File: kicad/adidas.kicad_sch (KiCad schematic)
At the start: 21 parts, among them J1 ISP Header, J2 Conn_01x02_Female, J3 SAO Header, U1 MPU-6050, U2 ATTINY841-SSU

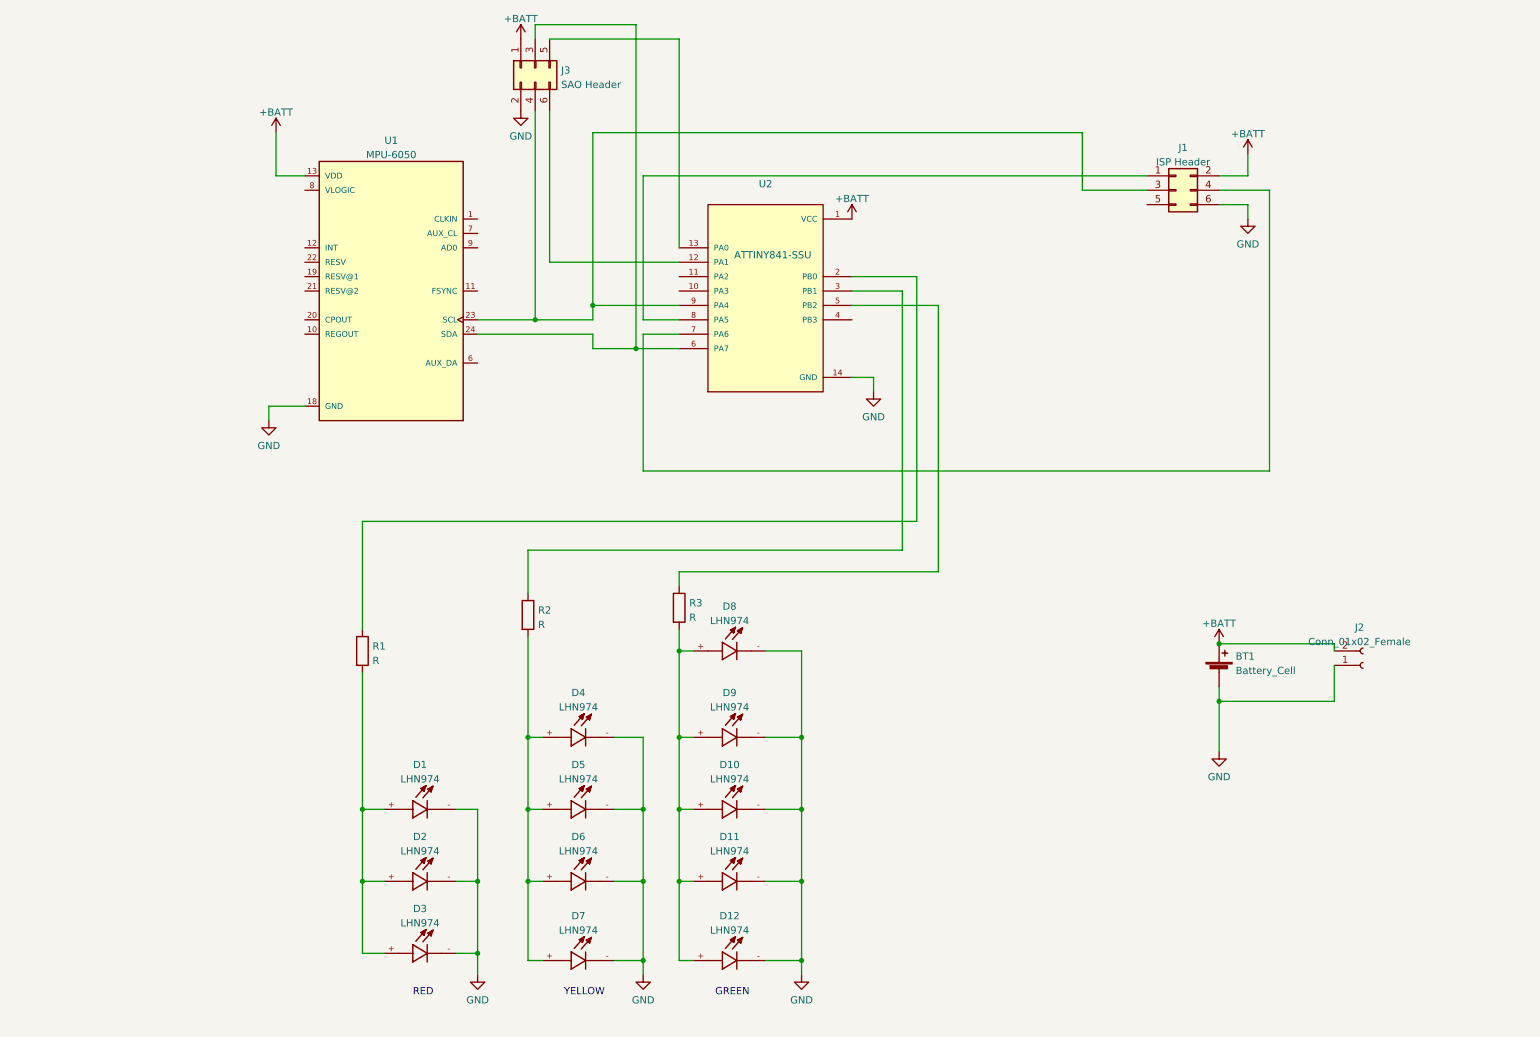
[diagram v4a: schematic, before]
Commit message: changes after feedback from PCBway
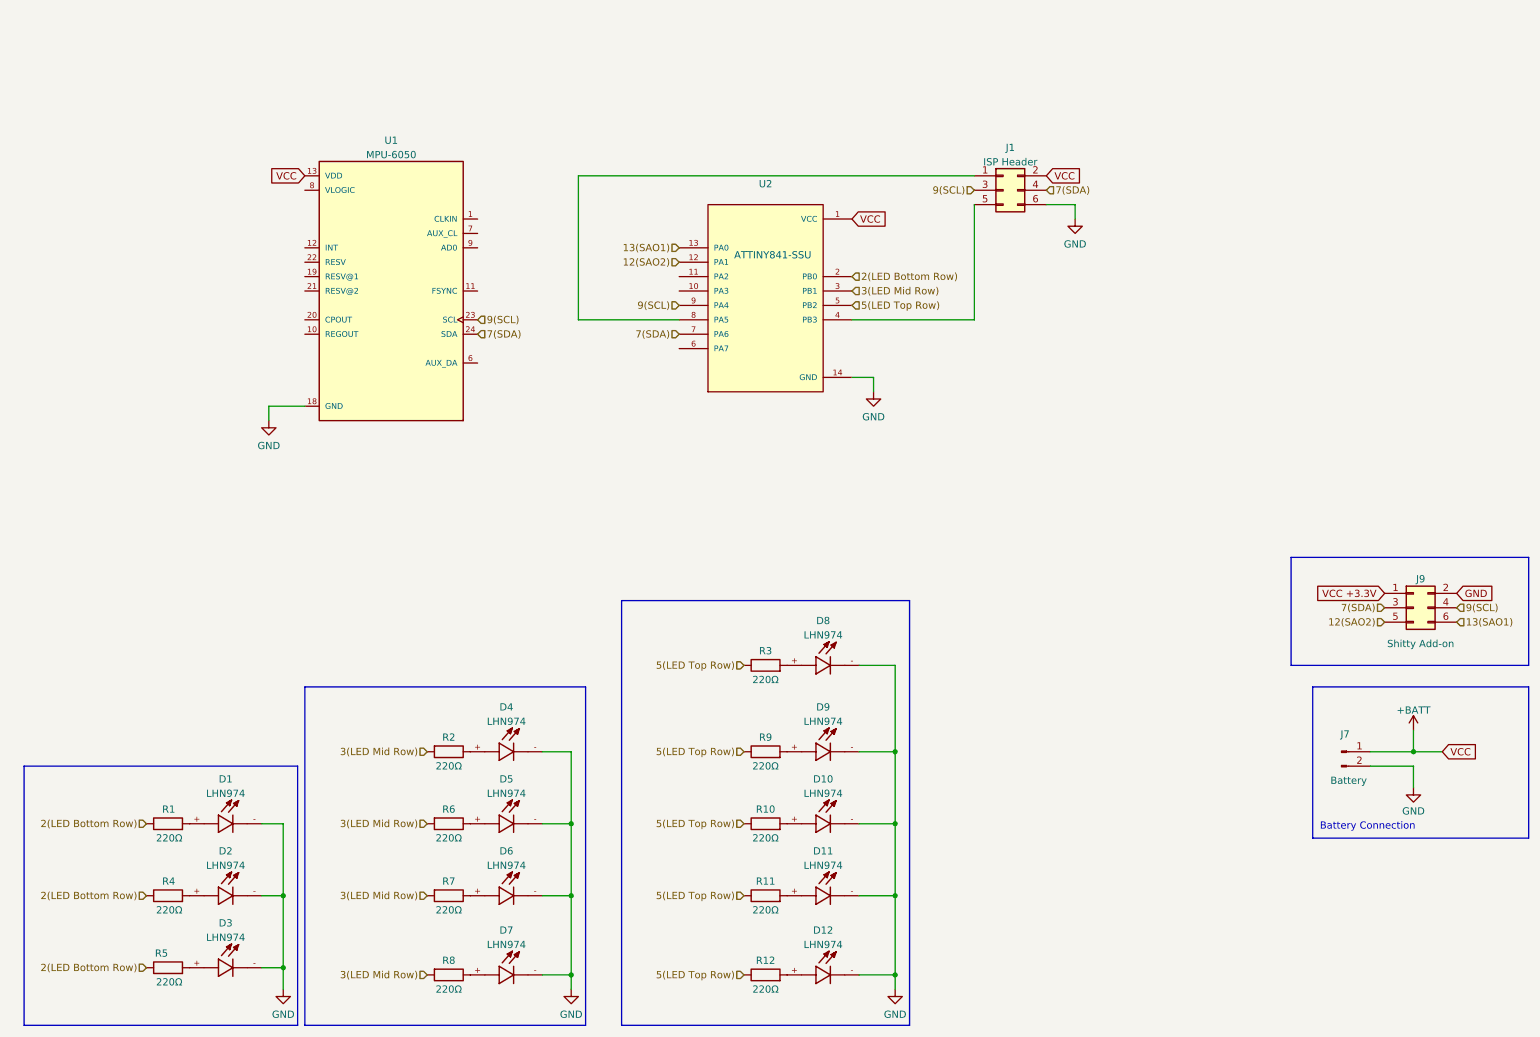
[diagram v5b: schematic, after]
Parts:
- removed BT1: Battery_Cell, Battery:BatteryHolder_Keystone_3002_1x2032, symbol Device:Battery_Cell
- removed J2: Conn_01x02_Female, TestPoint:TestPoint_2Pads_Pitch2.54mm_Drill0.8mm, symbol Connector:Conn_01x02_Female
- removed J3: SAO Header, Connector_PinHeader_2.54mm:PinHeader_2x03_P2.54mm_Vertical, symbol Connector_Generic:Conn_02x03_Odd_Even
- added J7: Battery, Connector_PinSocket_2.54mm:PinSocket_1x02_P2.54mm_Vertical, symbol Connector:Conn_01x02_Pin
- added J9: Shitty Add-on, Connector_PinHeader_2.54mm:PinHeader_2x03_P2.54mm_Vertical, symbol Connector_Generic:Conn_02x03_Odd_Even
- added R10, R11, R12, R4, R5, R6, R7, R8, R9: 220Ω, Resistor_SMD:R_1206_3216Metric, symbol Device:R
- D1, D10, D11, D12, D2, D3, D4, D5, D6, D7, D8, D9: footprint 1206_smt:LEDC3216X120N -> LED_SMD:LED_0805_2012Metric
- R1, R2, R3: value R -> 220Ω; footprint Resistor_SMD:R_1206_3216Metric_Pad1.30x1.75mm_HandSolder -> Resistor_SMD:R_1206_3216Metric
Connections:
- net +BATT: now also J7.1 (Pin_1)
- net GND: now also J7.2 (Pin_2), J9.2 (Pin_2)
- net 2(LED Bottom Row): now reaches R1.1, U2.2 (PB0)
- net 2(LED Bottom Row): now also R4.1, R5.1
- net at D1.+, R1.2: no longer D2.+, D3.+
- net at R2.1: now also D4.+; no longer U2.3 (PB1)
- net 9(SCL): now reaches J1.3 (Pin_3), U1.23 (SCL), U2.9 (PA4)
- net 9(SCL): now also J9.4 (Pin_4)
- net 7(SDA): now reaches J1.4 (Pin_4), U2.7 (PA6)
- net 7(SDA): now also U1.24 (SDA), J9.3 (Pin_3)
- net at J1.5 (Pin_5): now also U2.4 (PB3)
- net 5(LED Top Row): now reaches R3.1, U2.5 (PB2)
- net 5(LED Top Row): now also R10.1, R11.1, R12.1, R9.1
- net 12(SAO2): now reaches U2.12 (PA1)
- net 12(SAO2): now also J9.5 (Pin_5)
- net 13(SAO1): now reaches U2.13 (PA0)
- net 13(SAO1): now also J9.6 (Pin_6)
- net at U2.6 (PA7): no longer U1.24 (SDA)
- new net: D11.+, R11.2
- new net: D8.+, R3.2
- new net: D12.+, R12.2
- new net: D6.+, R7.1
- new net: D5.+, R6.1
- new net: D3.+, R5.2
- new net: D10.+, R10.2
- new net: D2.+, R4.2
- new net: D9.+, R9.2
- new net: D7.+, R8.1
- new net 3(LED Mid Row): R2.2, R6.2, R7.2, R8.2, U2.3 (PB1)
- new net VCC +3.3V: J9.1 (Pin_1)
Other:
- note added: "Battery Connection"
- note removed: "GREEN"
- note removed: "RED"
- note removed: "YELLOW"
- moved on the sheet: D1, D10, D11, D12, D2, D3, D4, D5, D6, D7, D8, D9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

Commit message: make more updates after PCBway feedback
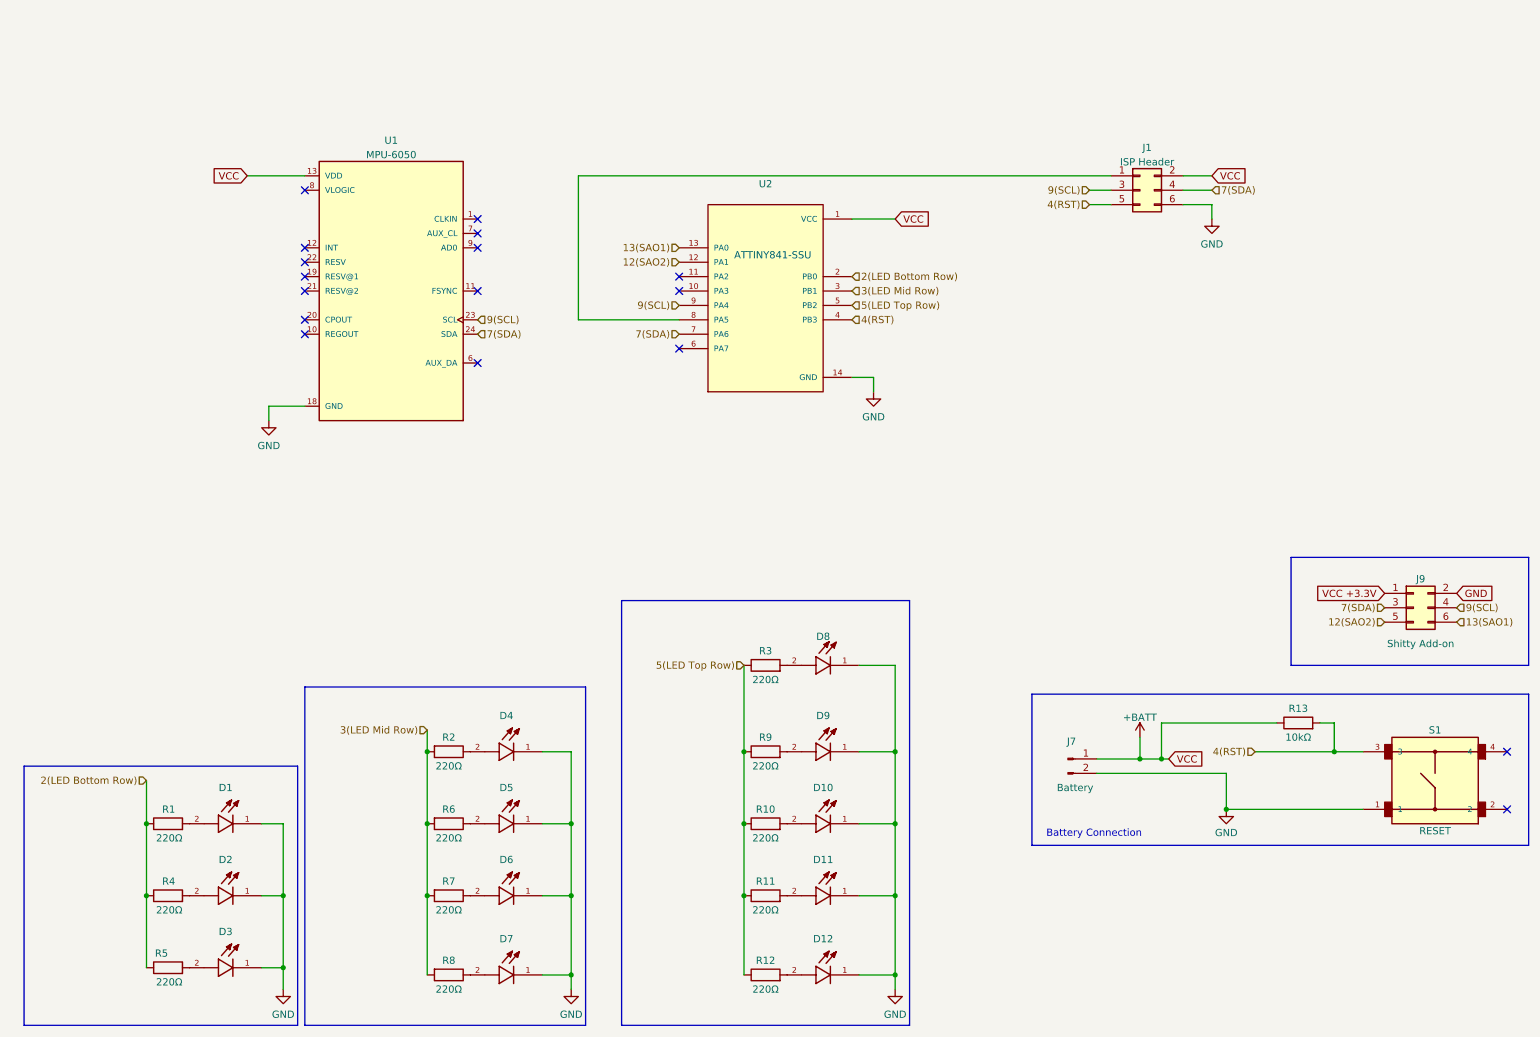
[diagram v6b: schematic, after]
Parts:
- added R13: 10kΩ, Resistor_SMD:R_1206_3216Metric, symbol Device:R
- added S1: B3F-1000, DEAD10C5:SW_B3F-1000, symbol dead10c5:B3F-1000
- D1, D10, D12, D2, D3, D4, D5, D6, D7, D8, D9: symbol LHN974:LHN974 -> dead10c5:LED-SMD-0805; MANUFACTURER Osram -> Valcon; MAXIMUM_PACKAGE_HEIGHT 1.20mm -> 0.8mm; PARTREV 2002-04-11 -> A; STANDARD IPC7-351B -> Manufacturer Recommendations
- D11: value LHN974 -> ~; symbol LHN974:LHN974 -> dead10c5:LED-SMD-0805; MANUFACTURER Osram -> Valcon; MAXIMUM_PACKAGE_HEIGHT 1.20mm -> 0.8mm; PARTREV 2002-04-11 -> A; STANDARD IPC7-351B -> Manufacturer Recommendations
- J1, J9: now left out of the parts list
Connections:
- net +BATT: now also R13.1
- net GND: now also D1.1, D10.1, D11.1, D12.1, D2.1, D3.1, D4.1, D5.1, D6.1, D7.1, D8.1, D9.1, S1.1; no longer D1.-, D10.-, D11.-, D12.-, D2.-, D3.-, D4.-, D5.-, D6.-, D7.-, D8.-, D9.-
- net at R1.2: now also D1.2; no longer D1.+
- net at R11.2: now also D11.2; no longer D11.+
- net at R3.2: now also D8.2; no longer D8.+
- net at R2.1: now also D4.2; no longer D4.+
- net at R12.2: now also D12.2; no longer D12.+
- net at R7.1: now also D6.2; no longer D6.+
- net at R6.1: now also D5.2; no longer D5.+
- net 4(RST): now reaches J1.5 (Pin_5), U2.4 (PB3)
- net 4(RST): now also R13.2, S1.3
- net at R5.2: now also D3.2; no longer D3.+
- net at R10.2: now also D10.2; no longer D10.+
- net at R4.2: now also D2.2; no longer D2.+
- net at R9.2: now also D9.2; no longer D9.+
- net at R8.1: now also D7.2; no longer D7.+
- no-connect marks 0 -> 17
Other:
- moved on the sheet: J1, J7
